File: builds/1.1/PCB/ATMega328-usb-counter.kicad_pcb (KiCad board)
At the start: 2 copper layers, 56 x 40 mm, 36 parts, among them J1 power, J2 PROG, J3 USB MINI, J4 RF, Q1 MMBT3904, U1 FT230XS, U2 ATmega328PB-AU, U3 74LV8154, X1 ABLNO

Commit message: rev 1.1 PCB
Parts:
- added H1: MountingHole, MountingHole:MountingHole_4.3mm_M4_Pad_Via, F.Cu at (63.6, 87.4)
- added H2: MountingHole, MountingHole:MountingHole_4.3mm_M4_Pad_Via, F.Cu at (113.0, 87.0)
- added H3: MountingHole, MountingHole:MountingHole_4.3mm_M4_Pad_Via, F.Cu at (113.2, 58.4)
- added J5: PROG, Connector_PinHeader_2.54mm:PinHeader_1x05_P2.54mm_Vertical, F.Cu at (111.8, 67.6)
- added R15: 50, Resistor_SMD:R_0805_2012Metric_Pad1.15x1.40mm_HandSolder, F.Cu at (72.6, 77.8)
- J3: value USB MINI -> USB_B_Micro; footprint Connector_USB:USB_Mini-B_Lumberg_2486_01_Horizontal -> Connector_USB:USB_Micro-B_Molex-105017-0001
- R14: value 10K -> 0
- R8: value 1K -> 0
- R9: value 10K -> 1k
- X1: value ABLNO -> TCXO
- moved R14 40.9 mm to (72.6, 81.6), turned to 180 degrees
- moved C3 34.5 mm to (85.8, 89.2), turned to 180 degrees
- moved D2 27.2 mm to (89.8, 75.2), turned to 0 degrees
- moved R3 22.9 mm to (93.8, 75.2), turned to 0 degrees
- moved R8 16.1 mm to (97.8, 75.2), turned to 0 degrees
- moved C7 8.81 mm to (105.0, 90.0), turned to 180 degrees
- moved J4 8.16 mm to (65.0, 77.6)
- moved C1 5.58 mm to (111.8, 64.6)
- moved J3 3.09 mm to (61.2, 66.7)
- moved R13 1.08 mm to (72.6, 85.8), turned to 180 degrees
- turned C9 to 270 degrees
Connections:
- net Net-(U3-Pad8) renamed OVF
- C3 pad 1: 3.3V -> Net-(C3-Pad1)
- C3 pad 2: GND -> Net-(C3-Pad2)
- C8 pad 1: RF-BUF -> COUNT
- C9 pad 2: Net-(C9-Pad2) -> Net-(C3-Pad2)
- D3 pad 2: Net-(C9-Pad1) -> Net-(C3-Pad2)
- D4 pad 1: Net-(C9-Pad1) -> Net-(C3-Pad2)
- J4 pad 1: Net-(J4-Pad1) -> SIGNAL
- Q1 pad 1: Net-(C9-Pad1) -> Net-(C3-Pad1)
- R10 pad 2: RF-BUF -> COUNT
- R11 pad 1: Net-(C9-Pad1) -> Net-(C3-Pad1)
- R12 pad 1: RF-BUF -> COUNT
- R13 pad 1: Net-(C9-Pad2) -> Net-(C9-Pad1)
- R13 pad 2: Net-(J4-Pad1) -> SIGNAL
- R14 pad 1: 10MHz -> COUNT
- R14 pad 2: Net-(R14-Pad2) -> SIGNAL
- R3 pad 2: Net-(R3-Pad2) -> GATE
- R8 pad 1: Net-(R8-Pad1) -> GATE
- R8 pad 2: GATE -> Net-(R8-Pad2)
- U2 pad 13: Net-(R3-Pad2) -> GATE
- U2 pad 14: GATE -> LCD-CS
- U2 pad 7: 10MHz -> Net-(U2-Pad7)
- U3 pad 1: Net-(U3-Pad1) -> COUNT
- U3 pad 11: Net-(R8-Pad1) -> 3.3V
- U3 pad 2: Net-(U3-Pad1) -> COUNT
- U3 pad 7: RF-BUF -> Net-(R8-Pad2)
- X1 pad 3: Net-(R14-Pad2) -> Net-(U2-Pad7)
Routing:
- net COUNT: track 0.00 -> 46.6 mm, vias 0 -> 2
- net SCK: track 12.3 -> 34.7 mm, vias 0 -> 2
- net LCD-CS: track 0.00 -> 20.1 mm, vias 0 -> 2
- net MOSI: track 9.19 -> 28.3 mm, vias 0 -> 2
- net 3.3V: track 125.0 -> 143.3 mm
- net Net-(R8-Pad2): track 0.00 -> 15.4 mm, vias 0 -> 2
- net SIGNAL: track 0.00 -> 12.8 mm
- net Net-(U2-Pad7): track 0.00 -> 12.5 mm, vias 0 -> 2
- net RF-BUF: track 11.8 -> 0.00 mm
- net GATE: track 28.7 -> 16.8 mm
- net Net-(C3-Pad2): track 0.00 -> 10.7 mm
- net Net-(R14-Pad2): track 10.7 -> 0.00 mm, vias 2 -> 0
- net Net-(R3-Pad2): track 9.85 -> 0.00 mm
- net Net-(C9-Pad1): track 13.0 -> 3.81 mm
- net Net-(C3-Pad1): track 0.00 -> 9.07 mm
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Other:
- board size 56 x 40 mm -> 60.6 x 40 mm
- board text added: "CK"
- board text added: "CS"
- board text added: "DAT"
- board text added: "INPUT"
- board text added: "USB COUNTER"
- board text added: "VCC"
- board text added: "rev1.1"
- board text removed: "10MHz"
- board text removed: "RF INPUT"
- board text removed: "STAT"
- board text removed: "USB FREQUENCY COUNTER"
- board text removed: "rev 1.0"

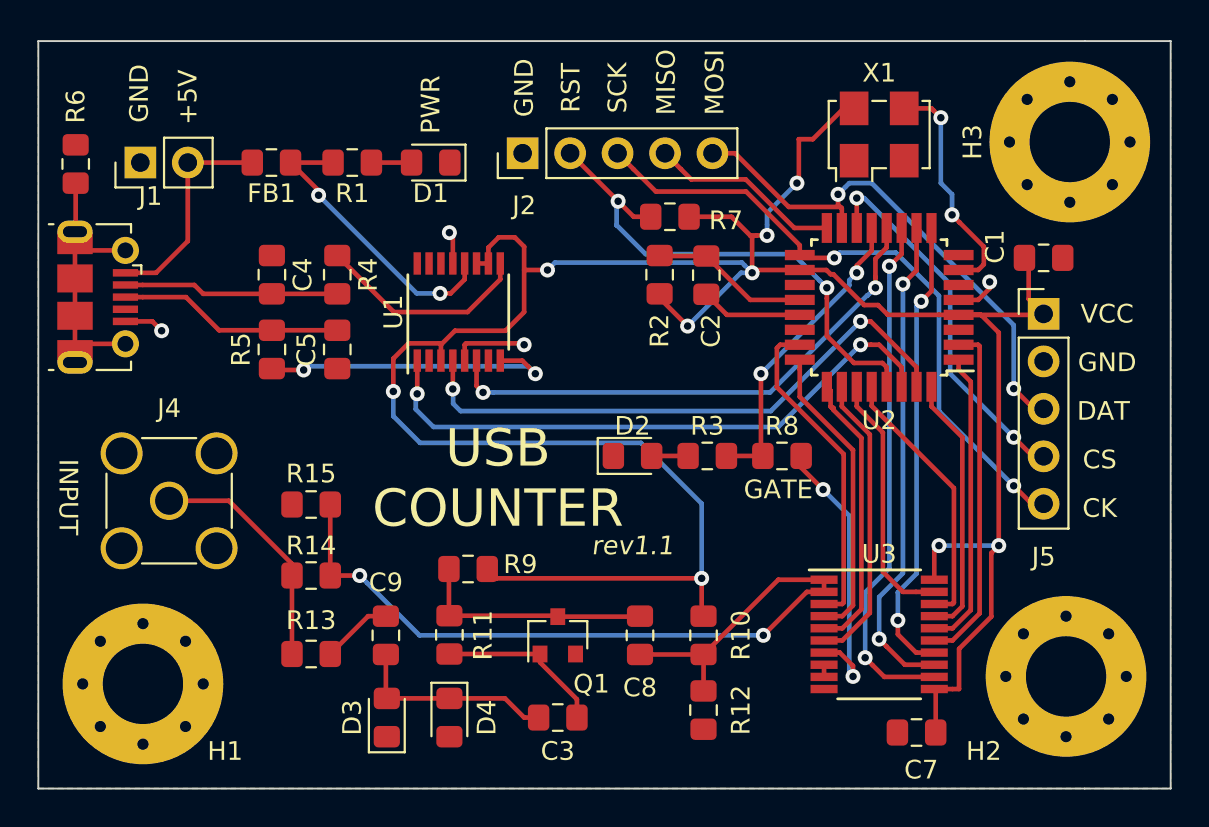
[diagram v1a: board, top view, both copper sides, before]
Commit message: added screw hole
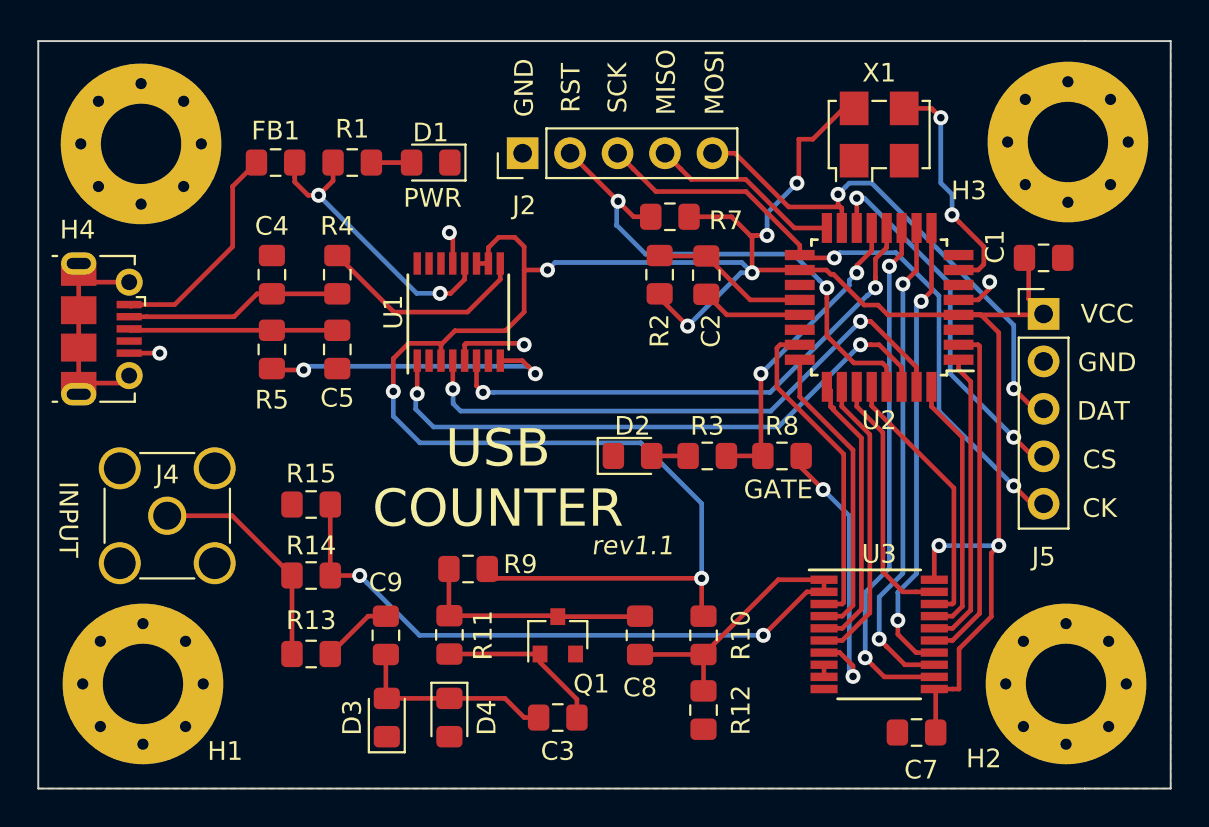
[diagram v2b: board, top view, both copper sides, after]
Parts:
- removed J1: power, Connector_PinHeader_2.54mm:PinHeader_1x02_P2.54mm_Vertical
- removed R6: 0, Resistor_SMD:R_0805_2012Metric_Pad1.15x1.40mm_HandSolder
- added H4: MountingHole, MountingHole:MountingHole_4.3mm_M4_Pad_Via, F.Cu at (63.5, 58.5)
- moved J3 1.71 mm to (61.4, 68.4)
- moved J4 0.81 mm to (64.9, 78.4)
- moved H2 0.40 mm to (113.0, 87.4)
- moved FB1 0.23 mm to (70.7, 59.5)
- moved H3 0.10 mm to (113.1, 58.4)
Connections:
- J3 pad 4: Net-(J3-Pad4) -> (no net)
- U1 pad 14: Net-(U1-Pad14) -> (no net)
- U1 pad 15: Net-(U1-Pad15) -> (no net)
- U1 pad 16: Net-(U1-Pad16) -> (no net)
- U1 pad 2: Net-(U1-Pad2) -> (no net)
- U1 pad 7: Net-(U1-Pad7) -> (no net)
- U2 pad 19: Net-(U2-Pad19) -> (no net)
- U2 pad 22: Net-(U2-Pad22) -> (no net)
- U2 pad 3: Net-(U2-Pad3) -> (no net)
- U2 pad 6: Net-(U2-Pad6) -> (no net)
- U2 pad 8: Net-(U2-Pad8) -> (no net)
- X1 pad 1: Net-(X1-Pad1) -> (no net)
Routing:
- net Net-(J3-Pad6): track 15.0 -> 12.3 mm
- net Net-(C5-Pad2): track 12.1 -> 11.2 mm
- net SIGNAL: track 12.8 -> 12.2 mm
- net GND: track 15.7 -> 15.2 mm
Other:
- board text removed: "+5V"

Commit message: improve silkscreen
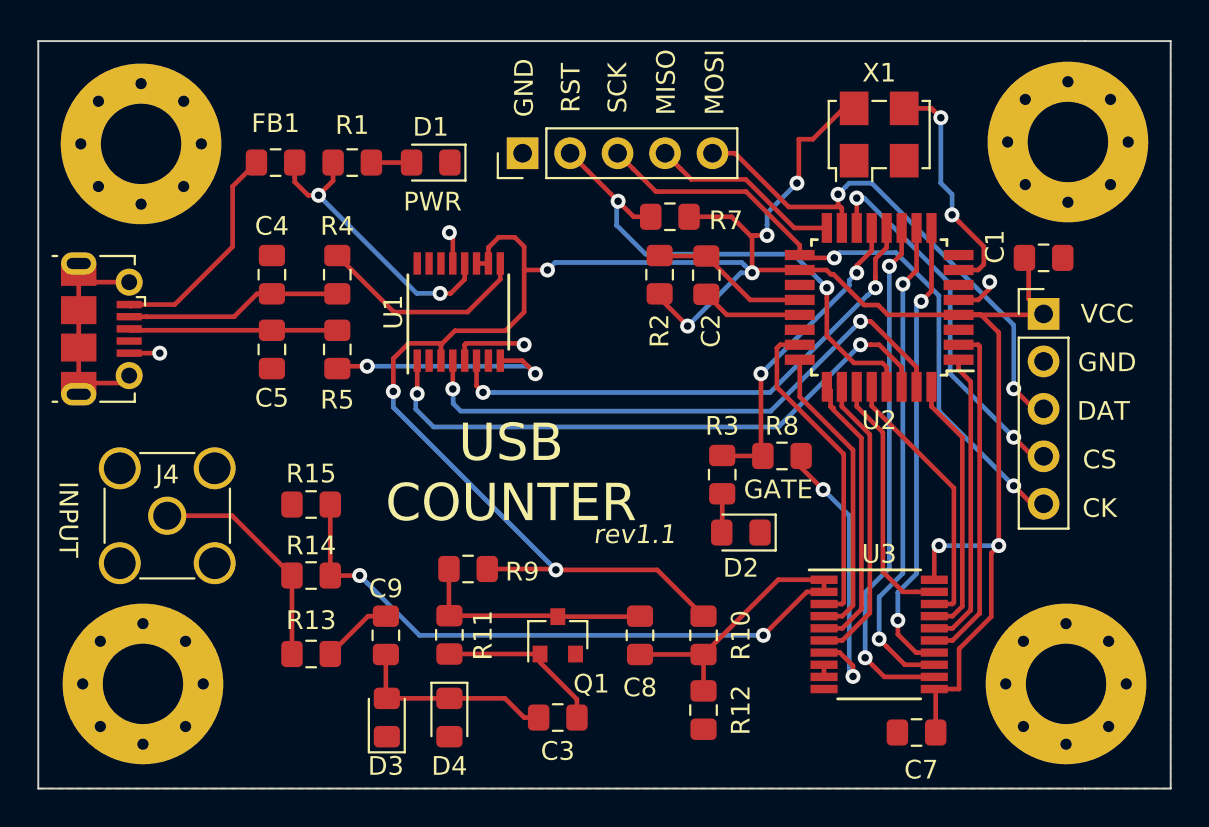
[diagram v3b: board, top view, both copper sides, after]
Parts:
- moved D2 7.10 mm to (95.6, 79.3), turned to 180 degrees
- moved C5 3.50 mm to (70.5, 69.5)
- moved R5 3.50 mm to (74.0, 69.5)
- moved R3 1.28 mm to (94.6, 76.2), turned to 90 degrees
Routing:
- net 3.3V: track 143.3 -> 131.6 mm
- net Net-(R5-Pad1): track 16.5 -> 13.0 mm

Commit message: new diode protection
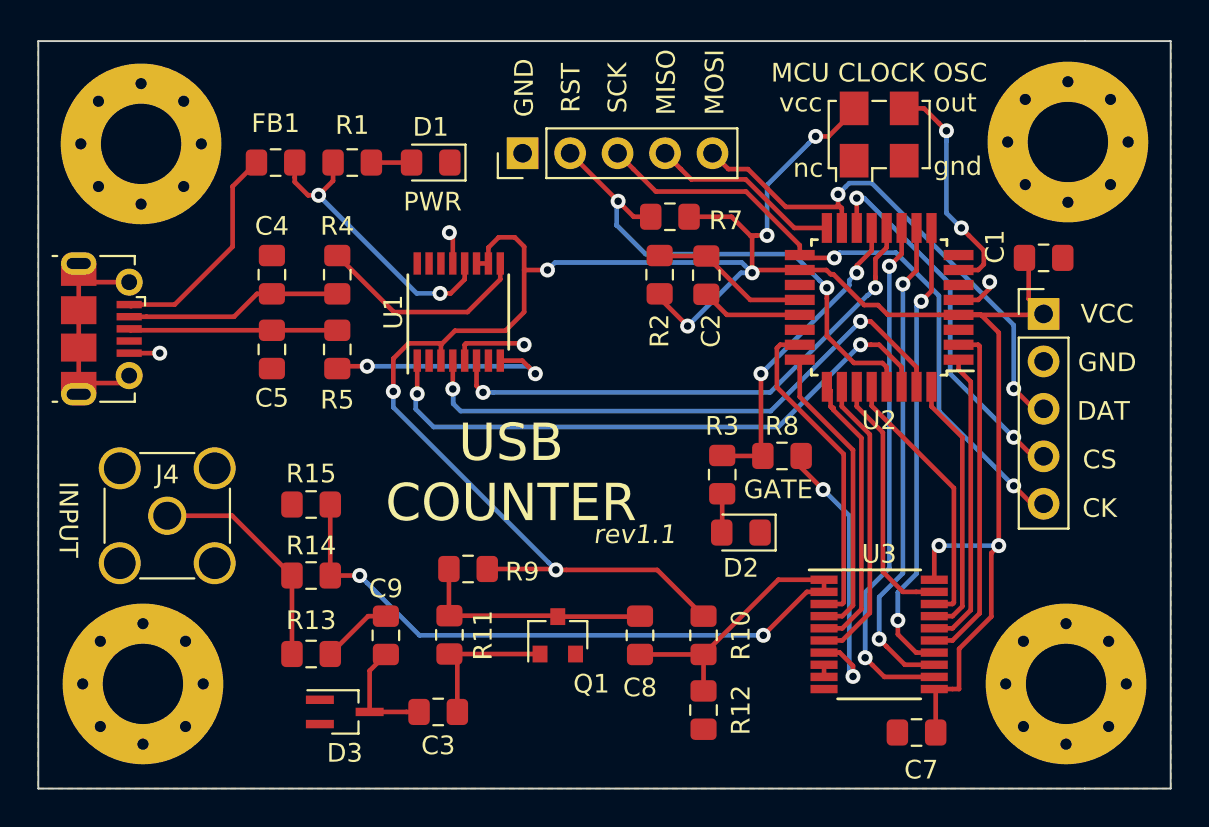
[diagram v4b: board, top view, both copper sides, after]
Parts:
- removed D4: D, Diode_SMD:D_0805_2012Metric_Pad1.15x1.40mm_HandSolder
- D3: value D -> BAV99WT1; footprint Diode_SMD:D_0805_2012Metric_Pad1.15x1.40mm_HandSolder -> Package_TO_SOT_SMD:SOT-323_SC-70_Handsoldering
- MCU CLOCK OSC: renamed from X1
- moved C3 6.41 mm to (79.4, 88.9)
- moved D3 2.27 mm to (74.4, 88.9), turned to 0 degrees
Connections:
- D3 pad 2: Net-(C3-Pad2) -> GND
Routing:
- net Net-(C3-Pad2): track 10.7 -> 6.08 mm
- net Net-(C3-Pad1): track 9.07 -> 8.13 mm
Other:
- board text added: "gnd"
- board text added: "nc"
- board text added: "out"
- board text added: "vcc"

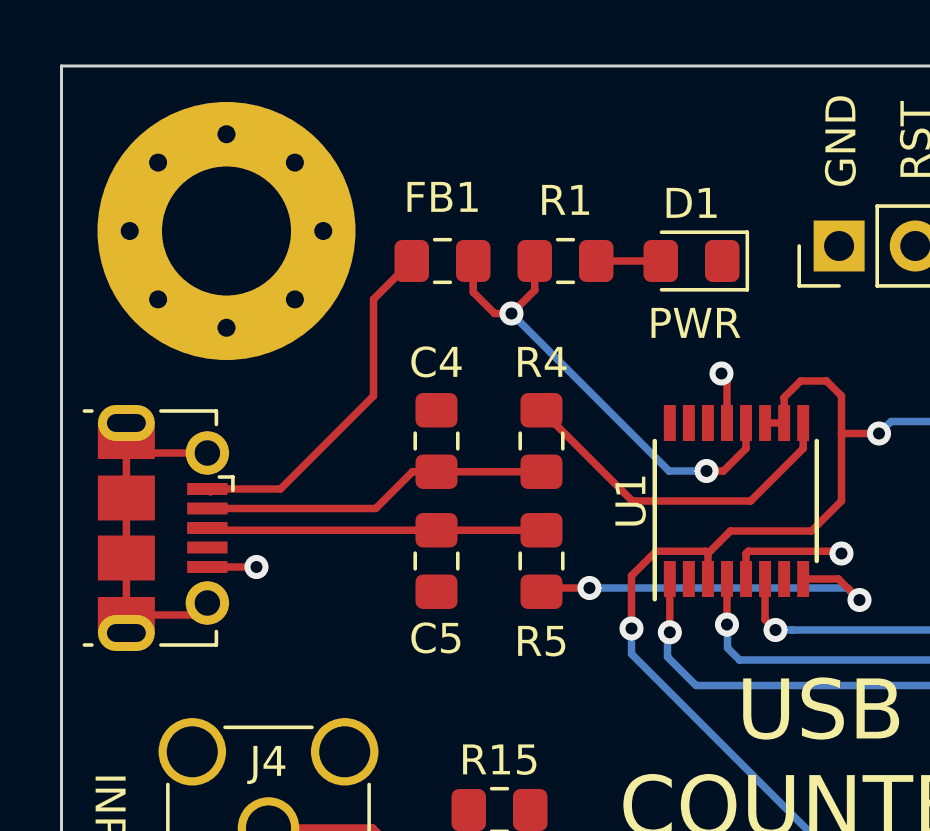
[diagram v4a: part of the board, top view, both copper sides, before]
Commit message: move usb connector to board edge
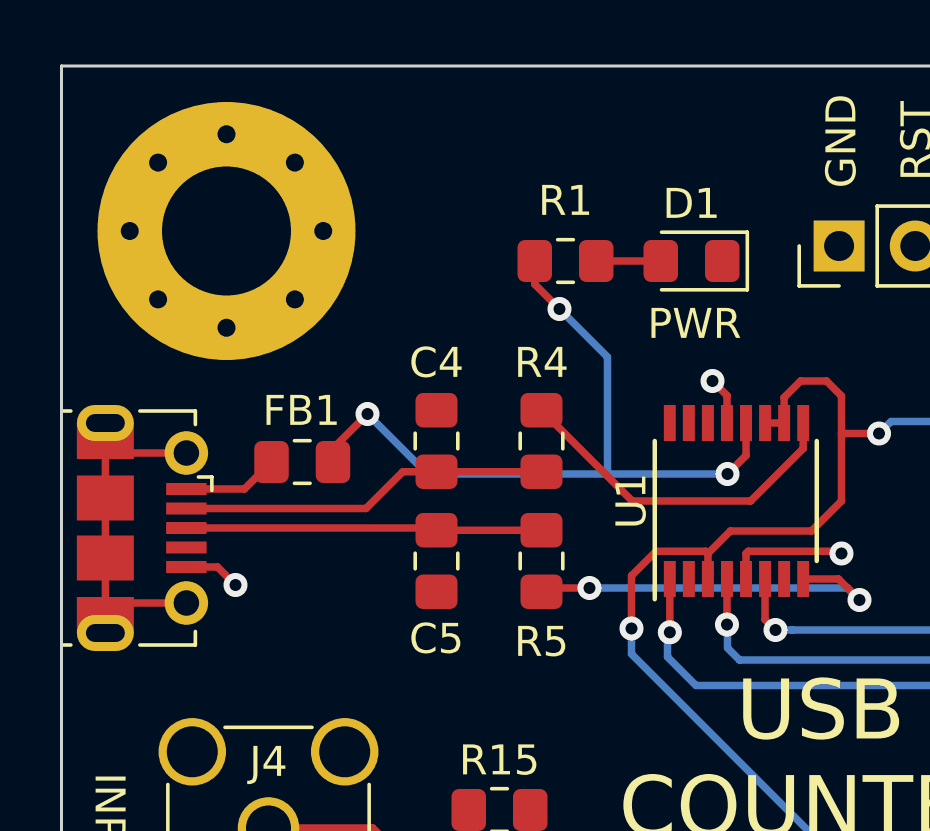
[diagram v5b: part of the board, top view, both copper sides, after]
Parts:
- moved FB1 8.17 mm to (66.0, 66.2)
- moved J3 0.70 mm to (60.7, 68.4)
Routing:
- net 5V: track 15.8 -> 25.0 mm, vias 2 -> 3
- net Net-(FB1-Pad2): track 12.0 -> 3.21 mm
- net Net-(J3-Pad6): track 12.3 -> 13.6 mm
- net Net-(C4-Pad2): track 11.6 -> 12.3 mm
- net Net-(C5-Pad2): track 11.2 -> 11.9 mm
